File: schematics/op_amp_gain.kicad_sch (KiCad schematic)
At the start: 7 parts, among them U6 TS971ILT

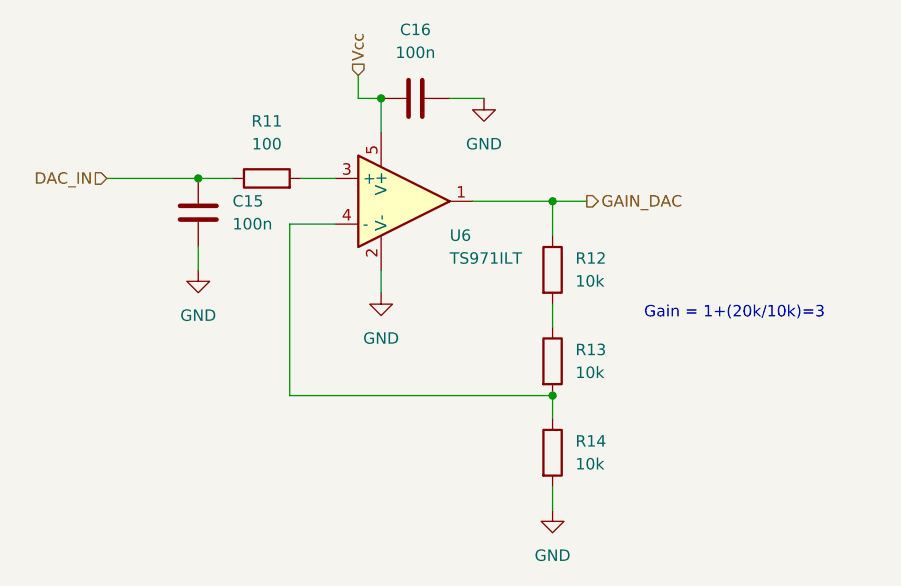
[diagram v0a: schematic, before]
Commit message: Added Rx board
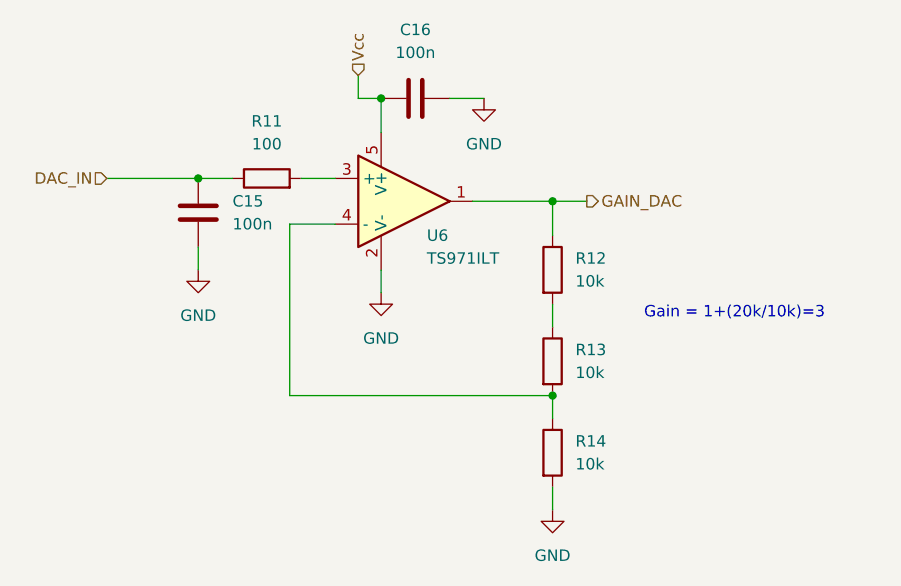
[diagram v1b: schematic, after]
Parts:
- C15, C16: Candidate (none) -> GRM155R71H104KE14D
- R11: footprint Resistor_SMD:R_01005_0402Metric -> Resistor_SMD:R_0402_1005Metric; Candidate (none) -> RC0402FR-7W100RL
- R12, R13, R14: footprint Resistor_SMD:R_01005_0402Metric -> Resistor_SMD:R_0402_1005Metric; Candidate (none) -> CRGP0402F10K
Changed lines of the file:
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@@
     (property "Reference" "R11" (id 0) (at 130.81 80.01 90))
     (property "Value" "100" (id 1) (at 130.81 82.55 90))
-    (property "Footprint" "Resistor_SMD:R_01005_0402Metric" (id 2) (at 130.81 88.138 90)
+    (property "Footprint" "Resistor_SMD:R_0402_1005Metric" (id 2) (at 130.81 88.138 90)
       (effects (font (size 1.27 1.27)) hide)
     )
     (property "Datasheet" "~" (id 3) (at 130.81 86.36 0)
+      (effects (font (size 1.27 1.27)) hide)
+    )
+    (property "Candidate" "RC0402FR-7W100RL" (id 4) (at 130.81 86.36 0)
       (effects (font (size 1.27 1.27)) hide)
     )
@@
       (effects (font (size 1.27 1.27)) (justify left))
     )
-    (property "Footprint" "Resistor_SMD:R_01005_0402Metric" (id 2) (at 160.782 96.52 90)
+    (property "Footprint" "Resistor_SMD:R_0402_1005Metric" (id 2) (at 160.782 96.52 90)
       (effects (font (size 1.27 1.27)) hide)
     )
     (property "Datasheet" "~" (id 3) (at 162.56 96.52 0)
+      (effects (font (size 1.27 1.27)) hide)
+    )
+    (property "Candidate" "CRGP0402F10K" (id 4) (at 162.56 96.52 0)
       (effects (font (size 1.27 1.27)) hide)
     )
@@
       (effects (font (size 1.27 1.27)) (justify left))
     )
-    (property "Footprint" "Resistor_SMD:R_01005_0402Metric" (id 2) (at 160.782 106.68 90)
+    (property "Footprint" "Resistor_SMD:R_0402_1005Metric" (id 2) (at 160.782 106.68 90)
       (effects (font (size 1.27 1.27)) hide)
     )
     (property "Datasheet" "~" (id 3) (at 162.56 106.68 0)
+      (effects (font (size 1.27 1.27)) hide)
+    )
+    (property "Candidate" "CRGP0402F10K" (id 4) (at 162.56 106.68 0)
       (effects (font (size 1.27 1.27)) hide)
     )
@@
       (effects (font (size 1.27 1.27)) (justify left))
     )
-    (property "Footprint" "Resistor_SMD:R_01005_0402Metric" (id 2) (at 160.782 116.84 90)
+    (property "Footprint" "Resistor_SMD:R_0402_1005Metric" (id 2) (at 160.782 116.84 90)
       (effects (font (size 1.27 1.27)) hide)
     )
     (property "Datasheet" "~" (id 3) (at 162.56 116.84 0)
+      (effects (font (size 1.27 1.27)) hide)
+    )
+    (property "Candidate" "CRGP0402F10K" (id 4) (at 162.56 116.84 0)
       (effects (font (size 1.27 1.27)) hide)
     )
@@
       (effects (font (size 1.27 1.27)) hide)
     )
+    (property "Candidate" "GRM155R71H104KE14D" (id 4) (at 123.19 90.17 0)
+      (effects (font (size 1.27 1.27)) hide)
+    )
     (pin "1")
     (pin "2")
@@
       (effects (font (size 1.27 1.27)) hide)
     )
+    (property "Candidate" "GRM155R71H104KE14D" (id 4) (at 147.32 77.47 0)
+      (effects (font (size 1.27 1.27)) hide)
+    )
     (pin "1")
     (pin "2")
@@
   (symbol (lib_id "User_library:TS971ILT") (at 146.05 88.9 0)
     (in_bom yes) (on_board yes)
-    (property "Reference" "U6" (id 0) (at 151.13 92.7099 0)
+    (property "Reference" "U6" (id 0) (at 148.59 92.7099 0)
       (effects (font (size 1.27 1.27)) (justify left))
     )
-    (property "Value" "TS971ILT" (id 1) (at 151.13 95.2499 0)
+    (property "Value" "TS971ILT" (id 1) (at 148.59 95.2499 0)
       (effects (font (size 1.27 1.27)) (justify left))
     )

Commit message: latest updates
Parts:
- renumbered C15 to C11, C16 to C12, R14 to R10, R11 to R7, R12 to R8, R13 to R9, U6 to U4
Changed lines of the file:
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@@
   (symbol (lib_id "power:GND") (at 123.19 96.52 0)
     (in_bom yes) (on_board yes) (fields_autoplaced)
-    (property "Reference" "#PWR038" (id 0) (at 123.19 102.87 0)
+    (property "Reference" "#PWR021" (id 0) (at 123.19 102.87 0)
       (effects (font (size 1.27 1.27)) hide)
     )
@@
   (symbol (lib_id "power:GND") (at 143.51 99.06 0)
     (in_bom yes) (on_board yes) (fields_autoplaced)
-    (property "Reference" "#PWR039" (id 0) (at 143.51 105.41 0)
+    (property "Reference" "#PWR023" (id 0) (at 143.51 105.41 0)
       (effects (font (size 1.27 1.27)) hide)
     )
@@
   (symbol (lib_id "power:GND") (at 154.94 77.47 0)
     (in_bom yes) (on_board yes) (fields_autoplaced)
-    (property "Reference" "#PWR040" (id 0) (at 154.94 83.82 0)
+    (property "Reference" "#PWR024" (id 0) (at 154.94 83.82 0)
       (effects (font (size 1.27 1.27)) hide)
     )
@@
   (symbol (lib_id "power:GND") (at 162.56 123.19 0)
     (in_bom yes) (on_board yes) (fields_autoplaced)
-    (property "Reference" "#PWR041" (id 0) (at 162.56 129.54 0)
+    (property "Reference" "#PWR025" (id 0) (at 162.56 129.54 0)
       (effects (font (size 1.27 1.27)) hide)
     )
@@
   (symbol (lib_id "Device:R") (at 130.81 86.36 90)
     (in_bom yes) (on_board yes) (fields_autoplaced)
-    (property "Reference" "R11" (id 0) (at 130.81 80.01 90))
+    (property "Reference" "R7" (id 0) (at 130.81 80.01 90))
     (property "Value" "100" (id 1) (at 130.81 82.55 90))
     (property "Footprint" "Resistor_SMD:R_0402_1005Metric" (id 2) (at 130.81 88.138 90)
@@
   (symbol (lib_id "Device:R") (at 162.56 96.52 0)
     (in_bom yes) (on_board yes) (fields_autoplaced)
-    (property "Reference" "R12" (id 0) (at 165.1 95.2499 0)
+    (property "Reference" "R8" (id 0) (at 165.1 95.2499 0)
       (effects (font (size 1.27 1.27)) (justify left))
     )
@@
   (symbol (lib_id "Device:R") (at 162.56 106.68 0)
     (in_bom yes) (on_board yes) (fields_autoplaced)
-    (property "Reference" "R13" (id 0) (at 165.1 105.4099 0)
+    (property "Reference" "R9" (id 0) (at 165.1 105.4099 0)
       (effects (font (size 1.27 1.27)) (justify left))
     )
@@
   (symbol (lib_id "Device:R") (at 162.56 116.84 0)
     (in_bom yes) (on_board yes) (fields_autoplaced)
-    (property "Reference" "R14" (id 0) (at 165.1 115.5699 0)
+    (property "Reference" "R10" (id 0) (at 165.1 115.5699 0)
       (effects (font (size 1.27 1.27)) (justify left))
     )
@@
   (symbol (lib_id "Device:C") (at 123.19 90.17 180)
     (in_bom yes) (on_board yes) (fields_autoplaced)
-    (property "Reference" "C15" (id 0) (at 127 88.8999 0)
+    (property "Reference" "C11" (id 0) (at 127 88.8999 0)
       (effects (font (size 1.27 1.27)) (justify right))
     )
@@
   (symbol (lib_id "Device:C") (at 147.32 77.47 90)
     (in_bom yes) (on_board yes) (fields_autoplaced)
-    (property "Reference" "C16" (id 0) (at 147.32 69.85 90))
+    (property "Reference" "C12" (id 0) (at 147.32 69.85 90))
     (property "Value" "100n" (id 1) (at 147.32 72.39 90))
     (property "Footprint" "Capacitor_SMD:C_0402_1005Metric" (id 2) (at 151.13 76.5048 0)
@@
   (symbol (lib_id "User_library:TS971ILT") (at 146.05 88.9 0)
     (in_bom yes) (on_board yes)
-    (property "Reference" "U6" (id 0) (at 148.59 92.7099 0)
+    (property "Reference" "U4" (id 0) (at 148.59 92.7099 0)
       (effects (font (size 1.27 1.27)) (justify left))
     )
